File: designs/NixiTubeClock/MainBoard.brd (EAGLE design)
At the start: 94 x 45 mm, 18 parts, among them IC1 LD117ADT-TR, J1 S2B-PH-SM4, J2 S2B-PH-SM4, J3 S2B-PH-SM4, J4 S2B-PH-SM4, J5 S2B-PH-SM4, J6 S2B-PH-SM4, J7 S2B-PH-SM4

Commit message: started work on mainboard
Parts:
- removed J3, J7: S2B-PH-SM4, CommonParts:JST_S2B-PH-SM4-TB(LF)(SN)
- added SV6: (no value), CommonParts:MA08-1
- J5: value S2B-PH-SM4 -> PJ-002AH-SMT-TR; device CommonParts:JST_S2B-PH-SM4-TB(LF)(SN) -> CommonParts:PJ-002AH-SMT-TR
- moved J1 56.5 mm to (21.0, 8.00)
- moved J2 56.5 mm to (12.0, 8.00)
- moved R1 56.5 mm to (16.5, 14.5)
- moved JP1 49.0 mm to (13.5, 32.5), turned to 180 degrees
- moved SV5 44.2 mm to (55.5, 17.5), turned to 90 degrees
- moved SV4 40.1 mm to (55.5, 40.5), turned to 90 degrees
- moved C1 33.1 mm to (-10.4, 14.3)
- moved C2 33.1 mm to (-10.4, 23.1)
- moved IC1 32.8 mm to (-16.3, 33.9)
- moved J5 31.5 mm to (77.0, -2.50), turned to 90 degrees
- moved SV2 18.8 mm to (29.5, 40.5), turned to 270 degrees
- moved SV3 15.4 mm to (29.5, 17.5), turned to 270 degrees
- moved SV1 10.8 mm to (49.0, 3.00)
- moved J4 8.50 mm to (86.0, 8.00), flipped to the top
- moved J6 8.50 mm to (77.0, 8.00), flipped to the top
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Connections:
- net 12V: no longer J3.2, J5.2
- net 170V: no longer J7.2
- net GND: no longer J3.1, J5.1, J7.1
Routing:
- net GND: track 235.6 -> 0.00 mm, vias 5 -> 0
- net 12V: track 130.2 -> 0.00 mm, vias 2 -> 0
- net 3.3V: track 99.2 -> 0.00 mm, vias 1 -> 0
- net RXD0: track 89.9 -> 0.00 mm, vias 3 -> 0
- net 5V: track 70.6 -> 0.00 mm, vias 1 -> 0
- net IO15: track 60.3 -> 0.00 mm, vias 1 -> 0
- net 170V: track 49.8 -> 0.00 mm, vias 2 -> 0
- net TXD0: track 43.3 -> 0.00 mm
- net IO4: track 18.6 -> 0.00 mm
- net IO5: track 17.9 -> 0.00 mm
- net IO2: track 8.36 -> 0.00 mm
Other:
- board size 94 x 45 mm -> 98 x 63 mm

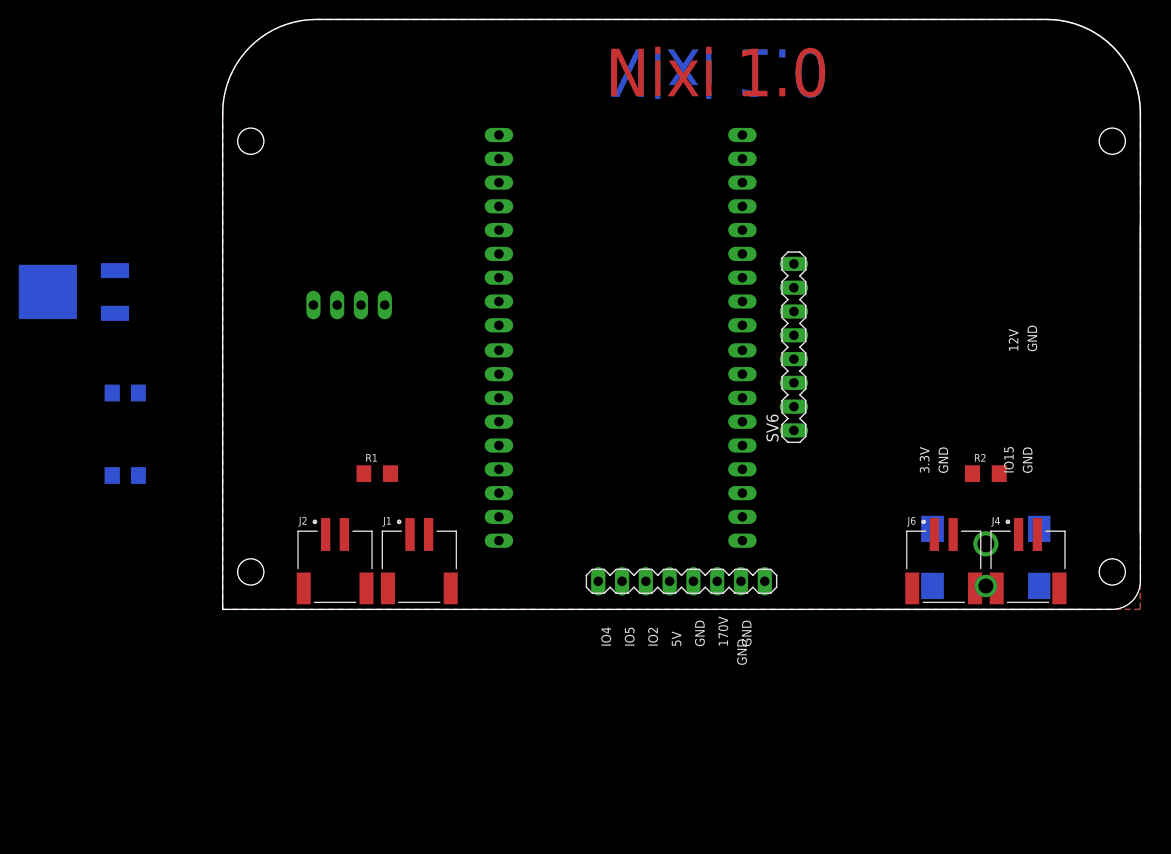
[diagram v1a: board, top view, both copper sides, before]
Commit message: added pinout on mainboard
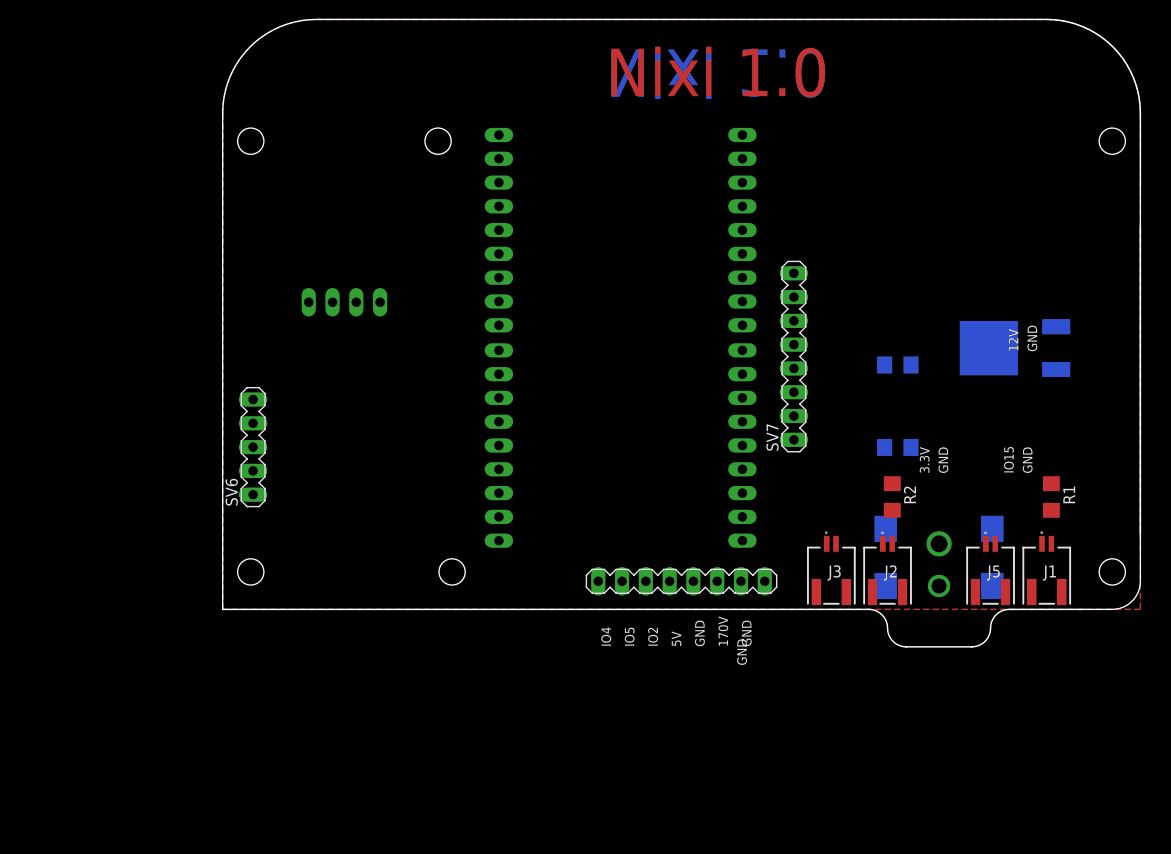
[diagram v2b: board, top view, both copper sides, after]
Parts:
- removed J6: S2B-PH-SM4, CommonParts:JST_S2B-PH-SM4-TB(LF)(SN)
- added J3: S2B-NSHSS-TB, CommonParts:SM02B-NSHSS-TB
- added SV7: (no value), CommonParts:MA08-1
- J1, J2: value S2B-PH-SM4 -> S2B-NSHSS-TB; device CommonParts:JST_S2B-PH-SM4-TB(LF)(SN) -> CommonParts:SM02B-NSHSS-TB
- J4: value S2B-PH-SM4 -> PJ-002AH-SMT-TR; device CommonParts:JST_S2B-PH-SM4-TB(LF)(SN) -> CommonParts:PJ-002AH-SMT-TR
- J5: value PJ-002AH-SMT-TR -> S2B-NSHSS-TB; device CommonParts:PJ-002AH-SMT-TR -> CommonParts:SM02B-NSHSS-TB
- SV6: device CommonParts:MA08-1 -> con-lstb:MA05-1
- moved IC1 100.7 mm to (84.2, 27.9)
- moved C1 82.6 mm to (72.1, 17.3)
- moved C2 82.6 mm to (72.1, 26.1)
- moved R1 72.0 mm to (88.5, 12.0), turned to 270 degrees
- moved J1 67.5 mm to (88.5, 7.00), turned to 180 degrees
- moved J2 59.5 mm to (71.5, 7.00), turned to 180 degrees
- moved SV6 58.7 mm to (3.25, 17.3)
- moved J4 17.5 mm to (72.0, -2.50), flipped to the bottom, turned to 90 degrees
- moved J5 11.0 mm to (82.5, 7.00), flipped to the top, turned to 180 degrees
- moved R2 10.3 mm to (71.5, 12.0), turned to 270 degrees
- moved JP1 0.58 mm to (13.0, 32.8)
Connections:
- net 3.3V: now also J2.2, J5.2; no longer J2.1, J6.1
- net GND: now also J1.1, J2.1, J3.1, J5.1; no longer J1.2, J2.2, J4.2, J6.2
- net IO15: now also J1.2; no longer J1.1
- net RXD0: now also J3.2; no longer J4.1
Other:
- board size 98 x 63 mm -> 98 x 67 mm

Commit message: added work to mainboard LEDs N-Channel Mosfet and names tNames
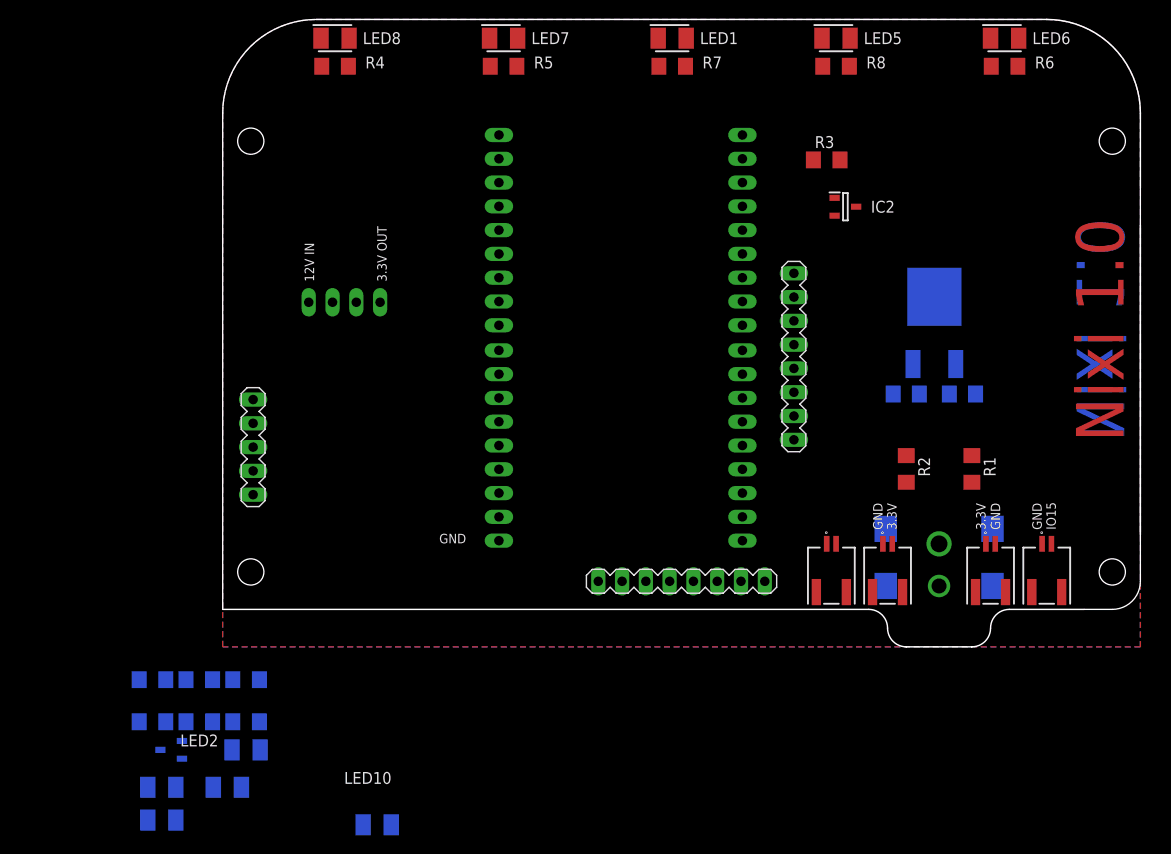
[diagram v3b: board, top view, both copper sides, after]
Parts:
- added IC2, IC3: FDN335N, CommonParts:SOT95P251X112-3N
- added LED1, LED10, LED2, LED3, LED4, LED5, LED6, LED7, LED8, LED9: PLCC2, CommonParts:LEDM3528X200N
- added R10, R11, R12, R13, R14, R3, R4, R5, R6, R7, R8, R9: (no value), CommonParts:R1206
- moved R1 9.01 mm to (80.0, 15.0)
- moved IC1 8.77 mm to (76.0, 31.0), turned to 0 degrees
- moved C2 7.56 mm to (79.0, 23.0), turned to 0 degrees
- moved C1 5.77 mm to (73.0, 23.0)
- moved R2 3.35 mm to (73.0, 15.0)
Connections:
- new net DS: SV6.5
- new net N$1: IC2.3, LED1.1, LED5.1, LED6.1, LED7.1, LED8.1
- new net N$10: LED3.2, R14.2
- new net N$11: LED2.2, R13.2
- new net N$12: LED4.2, R12.2
- new net N$13: LED9.2, R11.2
- new net N$14: LED10.2, R10.2
- new net N$2: IC2.1, R3.2
- new net N$3: LED5.2, R8.2
- new net N$4: LED1.2, R7.2
- new net N$5: LED6.2, R6.2
- new net N$6: LED7.2, R5.2
- new net N$7: LED8.2, R4.2
- new net N$8: IC3.1, R9.2
- new net N$9: IC3.3, LED10.1, LED2.1, LED3.1, LED4.1, LED9.1
- new net SCL: SV6.4
- new net SDA: SV6.3
- new net VCC: SV6.2
- net 12V: now also SV7.7, SV7.8
- net 170V: now also SV7.1, SV7.2
- net 3.3V: now also R10.1, R11.1, R12.1, R13.1, R14.1, R4.1, R5.1, R6.1, R7.1, R8.1
- net GND: now also R3.1, R9.1, SV6.1, SV7.3, SV7.4, SV7.5, SV7.6
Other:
- board text removed: "5V"

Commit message: further work on mainboard
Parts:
- moved LED9 123.5 mm to (84.5, 61.0)
- moved LED3 108.3 mm to (66.5, 61.0)
- moved IC3 108.2 mm to (83.5, 46.5), flipped to the top
- moved R11 104.9 mm to (84.5, 58.0)
- moved R9 97.9 mm to (73.5, 47.5), flipped to the top
- moved R14 94.8 mm to (66.5, 58.0)
- moved LED4 93.6 mm to (49.0, 61.0)
- moved R12 90.0 mm to (49.0, 58.0)
- moved LED10 85.2 mm to (31.0, 61.0)
- moved LED2 76.7 mm to (13.0, 61.0)
- moved R10 73.6 mm to (31.0, 58.0)
- moved R13 71.7 mm to (13.0, 58.0)
- moved IC2 18.4 mm to (83.5, 50.0)
- moved R3 9.49 mm to (73.5, 51.0)
- moved LED1 1.00 mm to (49.0, 61.0)
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
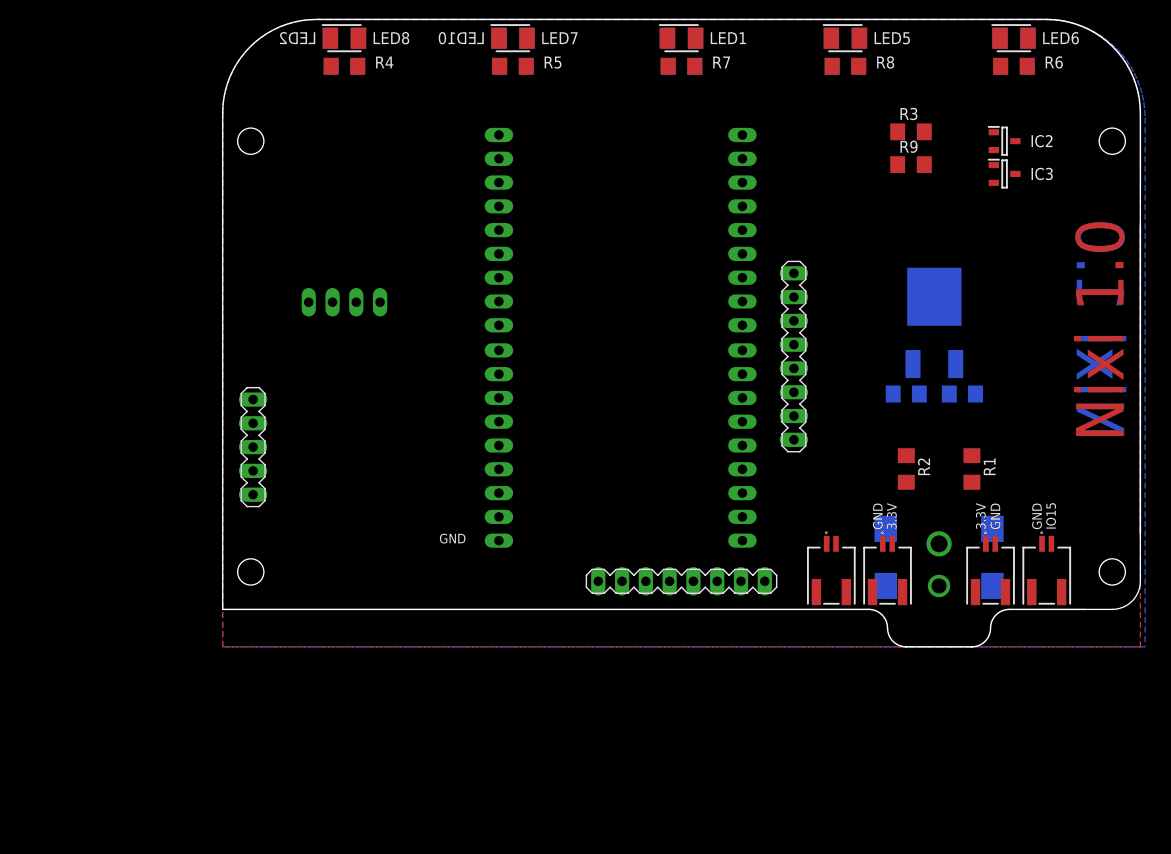
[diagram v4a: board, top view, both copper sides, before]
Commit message: added nixiClock brd and sheet with new design OSH
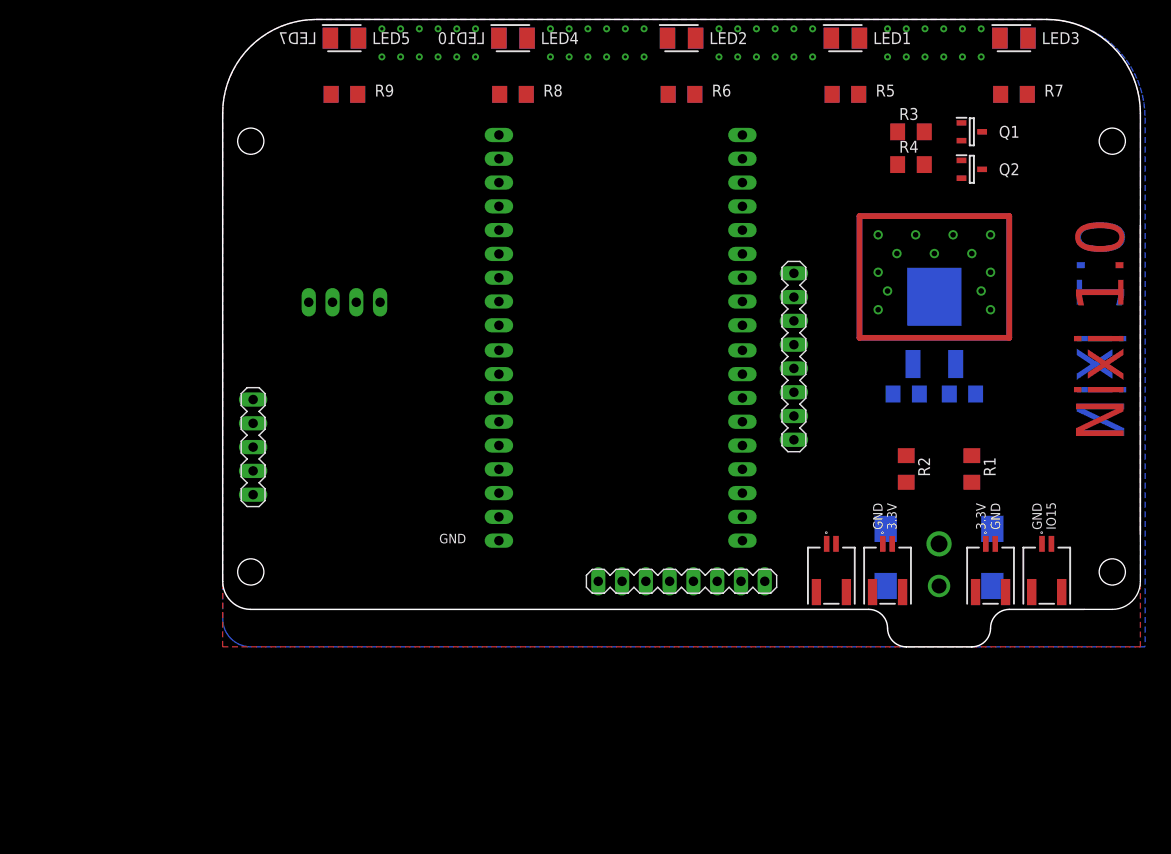
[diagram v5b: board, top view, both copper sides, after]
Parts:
- removed IC2, IC3: FDN335N, CommonParts:SOT95P251X112-3N
- added Q1, Q2: 2N7002NXAKR, CommonParts:SOT95P230X110-3N
- moved R11 71.6 mm to (13.0, 55.0)
- moved R13 71.6 mm to (84.5, 55.0)
- moved R4 61.4 mm to (73.5, 47.5)
- moved R9 61.0 mm to (13.0, 55.0)
- moved LED5 53.5 mm to (13.0, 61.0)
- moved LED2 36.0 mm to (49.0, 61.0), flipped to the top
- moved LED8 36.0 mm to (49.0, 61.0), flipped to the bottom
- moved R10 35.6 mm to (66.5, 55.0)
- moved R14 35.6 mm to (31.0, 55.0)
- moved R5 35.6 mm to (66.5, 55.0)
- moved R6 35.6 mm to (49.0, 55.0)
- moved R7 35.6 mm to (84.5, 55.0)
- moved R8 35.6 mm to (31.0, 55.0)
- moved LED3 18.0 mm to (84.5, 61.0), flipped to the top
- moved LED4 18.0 mm to (31.0, 61.0), flipped to the top
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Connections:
- removed net N$1: IC2.3, LED1.1, LED5.1, LED6.1, LED7.1, LED8.1
- new net N$28: LED1.1, LED2.1, LED3.1, LED4.1, LED5.1, Q1.3
- net 3.3V: now also R9.1; no longer R4.1
- net GND: now also Q1.2, Q2.2; no longer R3.1, R9.1
- net N$10: now also LED6.2, R10.2; no longer LED3.2, R14.2
- net N$11: now also LED7.2, R11.2; no longer LED2.2, R13.2
- net N$12: now also LED8.2; no longer LED4.2
- net N$13: now also R13.2; no longer R11.2
- net N$14: now also R14.2; no longer R10.2
- net N$2: now also Q1.1; no longer IC2.1
- net N$3: now also LED1.2, R5.2; no longer LED5.2, R8.2
- net N$4: now also LED2.2, R6.2; no longer LED1.2, R7.2
- net N$5: now also LED3.2, R7.2; no longer LED6.2, R6.2
- net N$6: now also LED4.2, R8.2; no longer LED7.2, R5.2
- net N$7: now also LED5.2, R9.2; no longer LED8.2, R4.2
- net N$8: now also Q2.1, R4.2; no longer IC3.1, R9.2
- net N$9: now also LED6.1, LED7.1, LED8.1, Q2.3; no longer IC3.3, LED2.1, LED3.1, LED4.1
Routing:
- net 5V: track 0.00 -> 116.0 mm
- added copper zone on layer 1, net 5V
- added copper zone on layer 16, net 5V
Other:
- outline, holes or cut-outs redrawn

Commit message: integrated T/H sensor
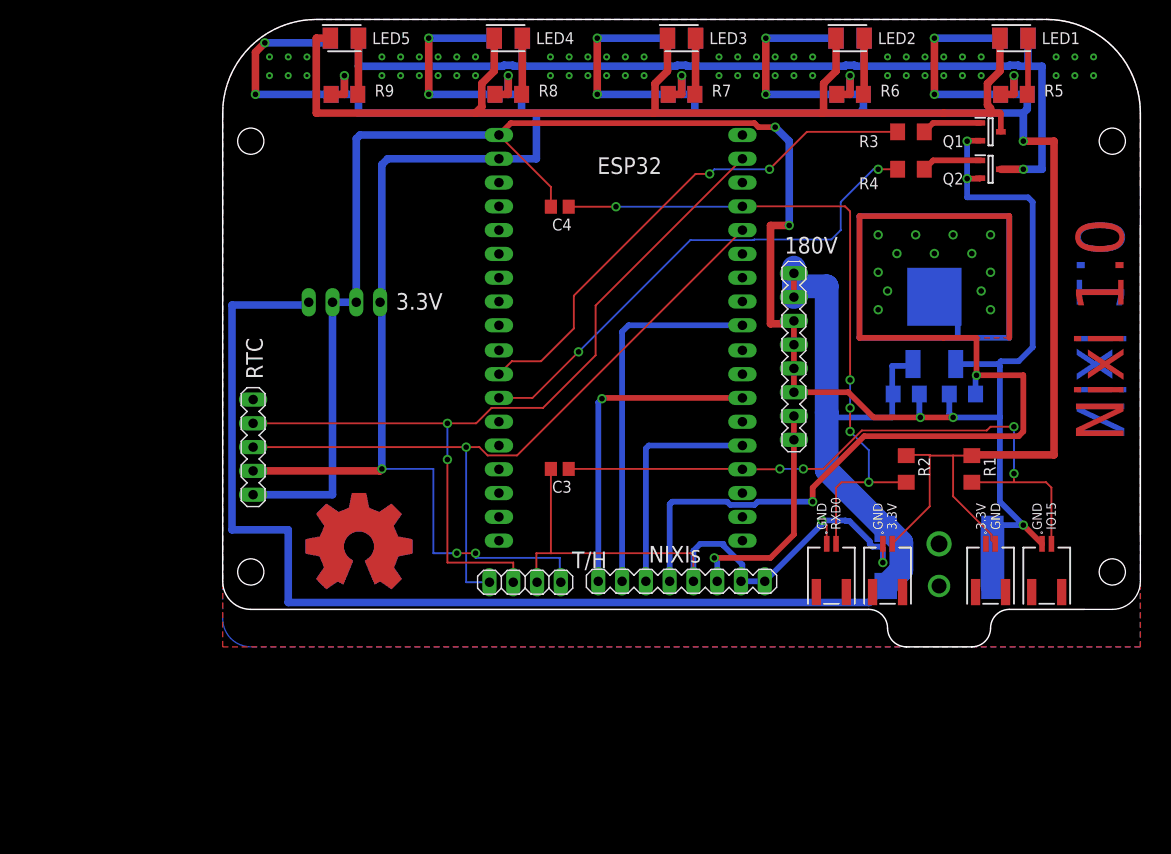
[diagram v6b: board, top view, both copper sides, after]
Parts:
- added C3, C4: 20nF, CommonParts:C0805
- added JP2: (no value), pinhead:1X04
- moved LED7 54.0 mm to (67.0, 61.0)
- moved LED9 54.0 mm to (30.5, 61.0)
- moved R11 54.0 mm to (67.0, 55.0)
- moved R13 54.0 mm to (30.5, 55.0)
- moved LED3 35.5 mm to (49.0, 61.0)
- moved R7 35.5 mm to (49.0, 55.0)
- moved SV4 23.0 mm to (55.5, 17.5), turned to 270 degrees
- moved SV5 23.0 mm to (55.5, 40.5), turned to 270 degrees
- moved LED1 18.0 mm to (84.5, 61.0)
- moved LED10 18.0 mm to (13.0, 61.0)
- moved LED2 18.0 mm to (67.0, 61.0)
- moved LED6 18.0 mm to (84.5, 61.0)
- moved R10 18.0 mm to (84.5, 55.0)
- moved R14 18.0 mm to (13.0, 55.0)
- moved R5 18.0 mm to (84.5, 55.0)
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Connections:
- removed net SCL: SV6.4
- removed net SDA: SV6.3
- removed net VCC: SV6.2
- net 12V: now also J4.3, J4.4
- net 3.3V: now also JP2.1, SV6.2
- net GND: now also C3.2, C4.2, J4.1, J4.2, JP2.2
- net IO15: now also C3.1
- net IO21: now also JP2.4, SV6.3
- net IO22: now also JP2.3, SV6.4
- net IO26: now also R3.1
- net IO27: now also R4.1
- net RXD0: now also C4.1
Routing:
- net GND: track 0.00 -> 312.5 mm, vias 1 -> 9
- net 3.3V: track 0.00 -> 293.2 mm, vias 0 -> 9
- net 12V: track 0.00 -> 171.1 mm
- net N$28: track 0.00 -> 119.3 mm
- net N$9: track 0.00 -> 103.7 mm, vias 0 -> 1
- net IO22: track 0.00 -> 91.2 mm, vias 0 -> 2
- net IO21: track 0.00 -> 79.7 mm, vias 0 -> 1
- net RXD0: track 0.00 -> 73.9 mm, vias 0 -> 5
- net IO15: track 0.00 -> 70.6 mm, vias 0 -> 4
- net 5V: track 116.0 -> 186.0 mm, vias 0 -> 15
- net IO26: track 0.00 -> 55.3 mm, vias 0 -> 2
- net IO27: track 0.00 -> 54.5 mm, vias 0 -> 2
- net IO5: track 0.00 -> 39.8 mm
- net IO4: track 0.00 -> 34.7 mm, vias 0 -> 1
- net 170V: track 0.00 -> 24.8 mm, vias 0 -> 1
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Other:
- board text added: "180V"
- board text added: "DS"
- board text added: "ESP32"
- board text added: "GPIO21"
- board text added: "GPIO22"
- board text added: "NIXIs"
- board text added: "RTC"
- board text added: "T/H"
- board text removed: "CMD"
